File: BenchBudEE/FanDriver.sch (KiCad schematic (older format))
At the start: 10 parts, among them Q2 MOSFET_N, Q3 MOSFET_N, Q4 MOSFET_N, U3 MCP4922-E/P, U4 OPA4170

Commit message: Arduino module associated + roughly placed.
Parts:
- U4: Distributor (none) -> DigiKey; Distributor Part Link (none) -> www.digikey.com/product-detail/en/OPA4170AIDR/296-29664-1-N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; Distributor Part Number (none) -> 296-29664-1-ND; MFG Name (none) -> Texas Instruments; MFG Part Number (none) -> OPA4170AIDR
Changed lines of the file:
@@
 Sheet 6 9
 Title ""
-Date "20 feb 2014"
+Date "23 feb 2014"
 Rev ""
 Comp ""
@@
 F 1 "OPA4170" H 6300 1850 50  0000 C CNN
 F 2 "" H 6150 2050 60  0000 C CNN
-F 3 "" H 6150 2050 60  0000 C CNN
+F 3 "http://www.ti.com/lit/ds/symlink/opa4170.pdf" H 6150 2050 60  0001 C CNN
+F 4 "Texas Instruments" H 6150 2050 60  0001 C CNN "MFG Name"
+F 5 "OPA4170AIDR" H 6150 2050 60  0001 C CNN "MFG Part Number"
+F 6 "DigiKey" H 6150 2050 60  0001 C CNN "Distributor"
+F 7 "296-29664-1-ND" H 6150 2050 60  0001 C CNN "Distributor Part Number"
+F 8 "www.digikey.com/product-detail/en/OPA4170AIDR/296-29664-1-ND/2762167" H 6150 2050 60  0001 C CNN "Distributor Part Link"
 	3    6150 2050
 	1    0    0    -1

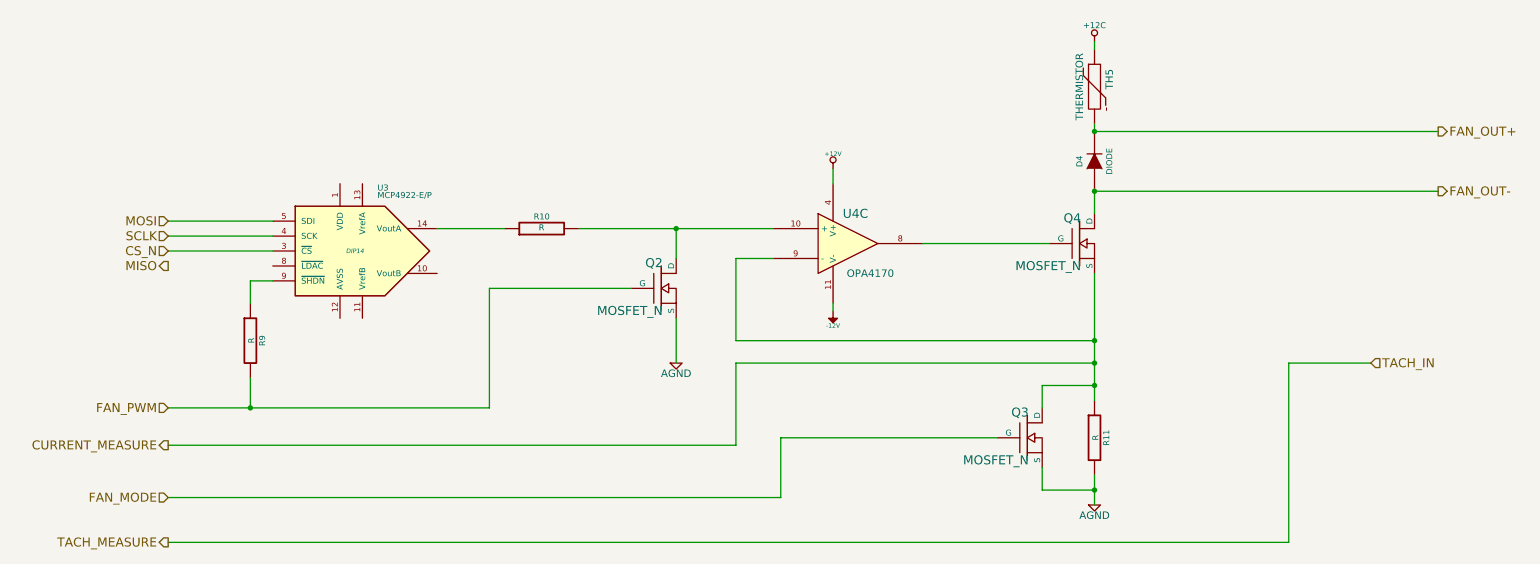
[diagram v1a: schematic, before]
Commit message: Fan/Current driver associated + roughly placed.
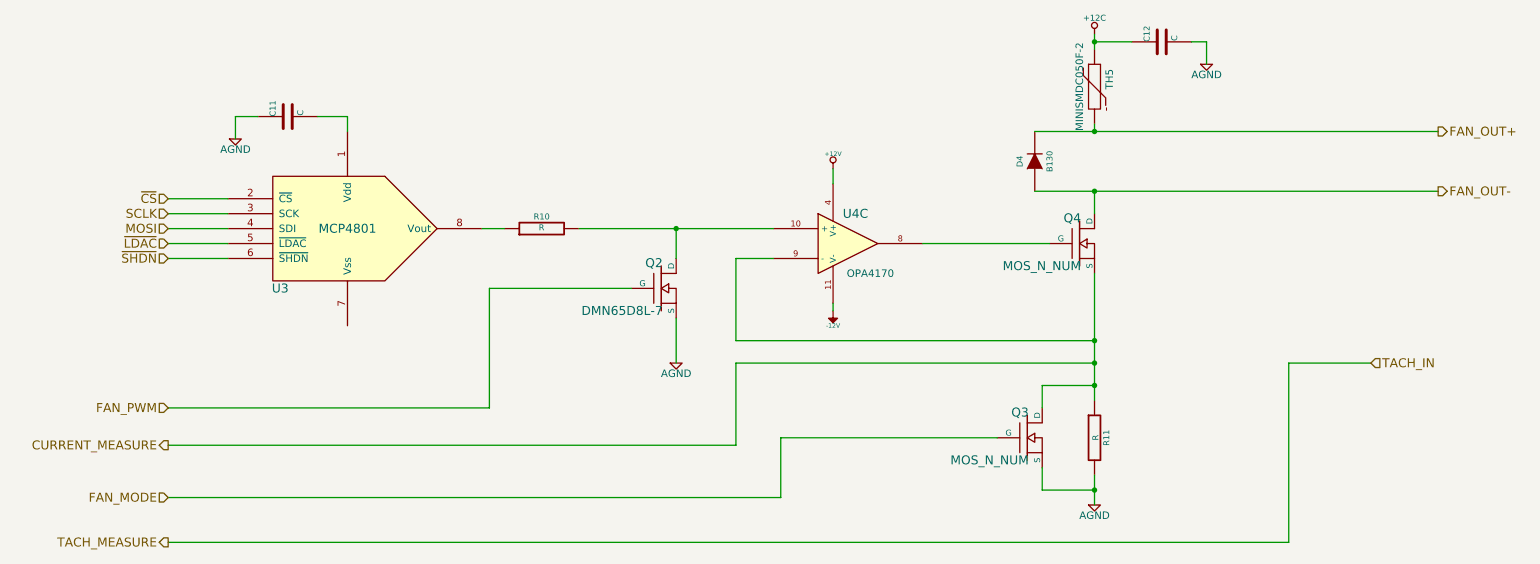
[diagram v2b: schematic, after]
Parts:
- removed Q3, Q4: MOSFET_N, ~, symbol MOSFET_N
- removed R9: R, ~, symbol R
- removed U3: MCP4922-E/P, DIP14, symbol MCP4922-E/P
- added C11, C12: C, ~, symbol C
- added Q3, Q4: MOS_N_NUM, ~, symbol MOS_N_NUM
- added U3: MCP4801, ~, symbol MCP4801
- D4: value DIODE -> B130; Distributor (none) -> DigiKey; Distributor Part Link (none) -> http://www.digikey.com/product-detail/en/B130-13-F/B130-FDI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; Distributor Part Number (none) -> B130-FDICT-ND; MFG Name (none) -> Diodes Incorporated; MFG Part Number (none) -> B130-13-F
- Q2: value MOSFET_N -> DMN65D8L-7; Distributor (none) -> DigiKey; Distributor Part Link (none) -> http://www.digikey.com/product-detail/en/DMN65D8L-7/DMN65D8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; Distributor Part Number (none) -> DMN65D8L-7DICT-ND; MFG Name (none) -> Diodes Incorporated; MFG Part Number (none) -> DMN65D8L-7
- TH5: value THERMISTOR -> MINISMDC050F-2; Distributor (none) -> DigiKey; Distributor Part Link (none) -> http://www.digikey.com/product-detail/en/MINISMDC050F-2/MIN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; Distributor Part Number (none) -> MINISMDC050FCT-ND; MFG Name (none) -> TE Connectivity; MFG Part Number (none) -> MINISMDC050F-2
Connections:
- net +12C: now also C12.1
- net AGND: now also C11.1, C12.2, Q3.3 (S)
- net CURRENT_MEASURE: now also Q3.2 (D), Q4.3 (S)
- net FAN_MODE: now also Q3.1 (G)
- net FAN_OUT-: now also Q4.2 (D)
- net MOSI: now also U3.4 (SDI)
- net SCLK: now also U3.3 (SCK)
- net at U4.8: now also Q4.1 (G)
- net at R10.1: now also U3.8 (Vout)
- new net: C11.2, U3.1 (Vdd)
- new net ~CS: U3.2 (~CS)
- new net ~LDAC: U3.5 (~LDAC)
- new net ~SHDN: U3.6 (~SHDN)
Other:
- moved on the sheet: D4
